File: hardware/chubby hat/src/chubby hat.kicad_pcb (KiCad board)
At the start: 2 copper layers, 143.5 x 91.4 mm, 84 parts, among them J1 HUB75, J10 Conn_01x02, J11 Conn_01x04, J12 USB_C_Receptacle_USB2.0, J13 Conn_ARM_JTAG_SWD_10, J14 SWD, J15 5V, J16 5V, J17 5V, J18 5V, J19 5V, J2 HUB75, J20 Conn_ARM_JTAG_SWD_10, J21 TC2030, J3 HUB75, J4 HUB75, J5 HUB75, J6 HUB75, J7 HUB75, J8 HUB75, J9 Screw_Terminal_01x02, Q1 AO3401A, SW2 reset, SW3 boot0, U1 FT2232D, U2 USBLC6-2SC6, U3 STM32F103C8Tx, U4 AMS1117-3.3, Y1 6MHz, Y2 8MHz

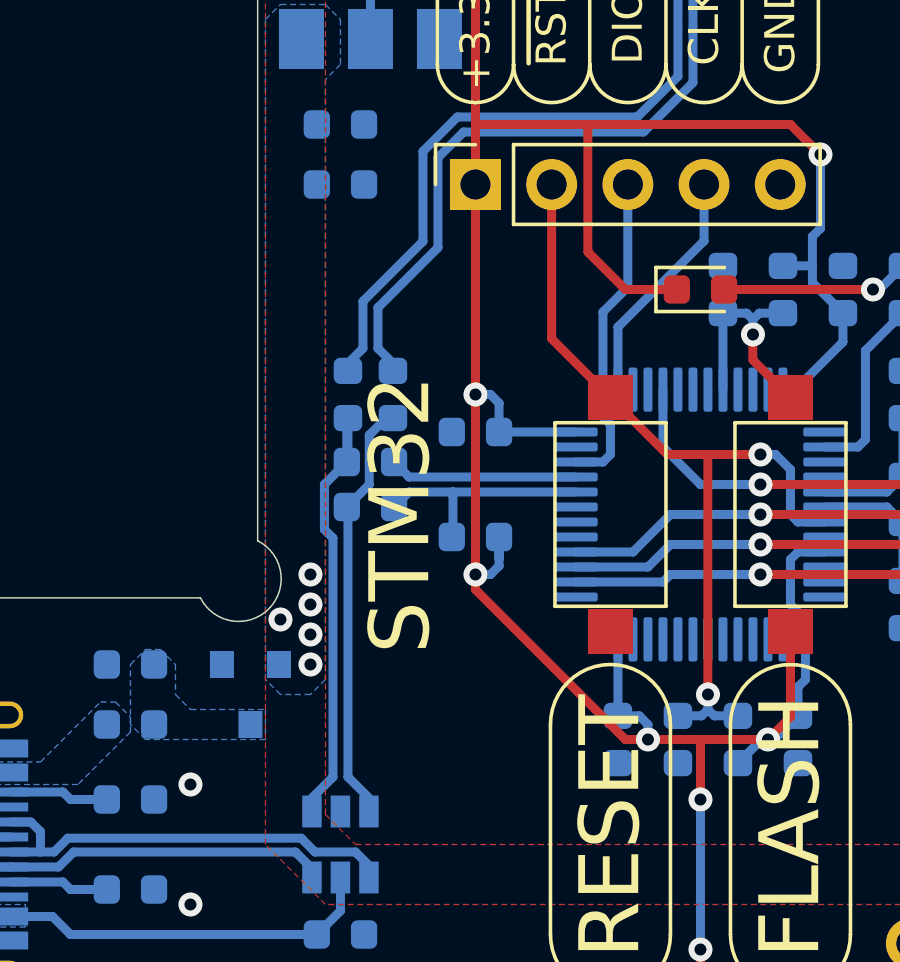
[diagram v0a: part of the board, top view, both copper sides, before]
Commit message: fix STM32 USB; closes #2
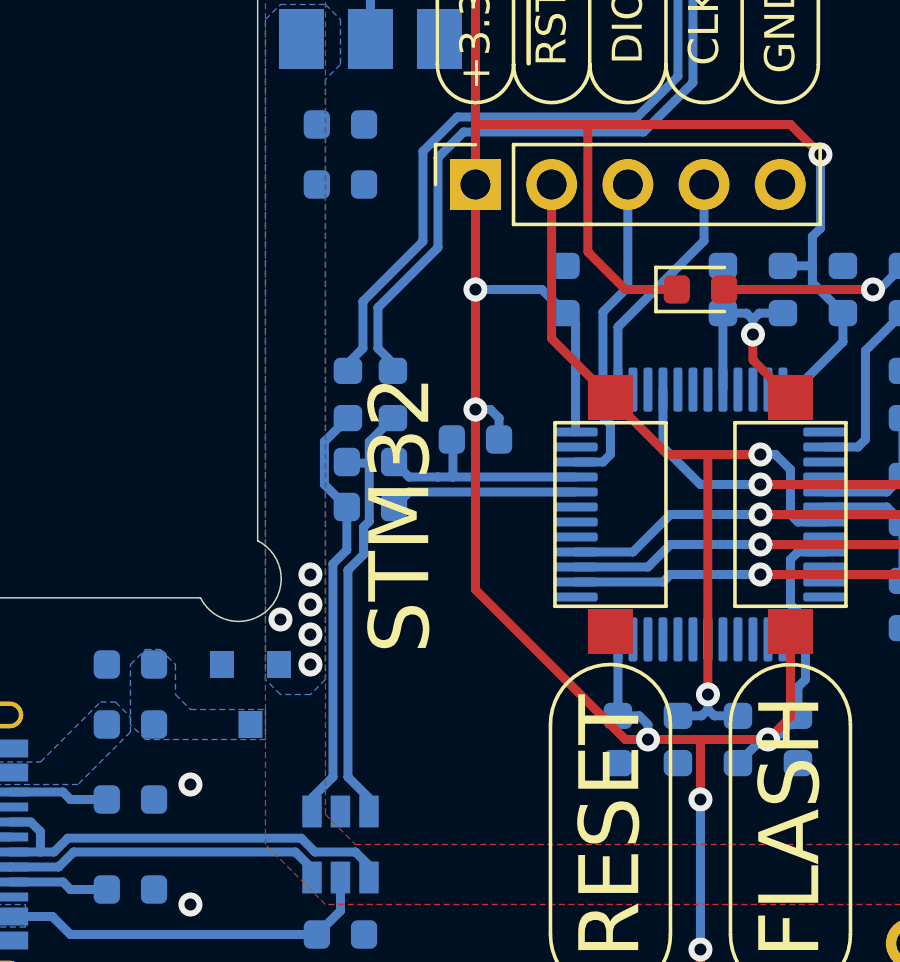
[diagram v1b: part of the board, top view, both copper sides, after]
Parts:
- moved C11 5.62 mm to (152.5, 88.8), turned to -90 degrees
- moved R12 3.25 mm to (149.5, 93.8)
- moved R6 1.50 mm to (146.0, 94.5)
- moved R7 1.50 mm to (146.0, 96.0)
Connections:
- U3 pad 32: /Blue Pill/D_P -> /Blue Pill/D_N
- U3 pad 33: /Blue Pill/D_N -> /Blue Pill/D_P
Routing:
- net +3V3: track 402.0 -> 404.3 mm
- net /USB.D+: track 13.5 -> 14.3 mm
- net /USB.D-: track 14.6 -> 13.8 mm
